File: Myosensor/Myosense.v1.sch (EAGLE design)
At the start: 22 parts, among them IC1 LM358D, IC2 LM358D, IC3 LM358D

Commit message: Worked on myosensor
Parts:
- added JP1: (no value), 3DPC:PINHD-1X2/90
- added OUTPUT: (no value), pinhead:PINHD-1X1
- added SENSOR1, SENSOR2: (no value), pinhead:PINHD-1X2
- IC1, IC2, IC3: value LM358D -> LM358N; device linear:LM358D -> 3DPC:LM358N
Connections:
- net N$9 renamed V2
- new net GND\: SENSOR2.2
- new net V+: IC1P.V+, IC2P.V+, IC3P.V+, JP1.1
- new net V1: IC1A.+IN, SENSOR1.1
- net GND: now also IC1P.V-, IC2P.V-, IC3P.V-, JP1.2, SENSOR1.2
- net N$17: now also OUTPUT.1
- net N$8: now also SENSOR2.1; no longer IC1A.+IN
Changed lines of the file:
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@@
 <layers>
 <layer number="1" name="Top" color="4" fill="1" visible="no" active="no"/>
+<layer number="2" name="Route2" color="1" fill="3" visible="no" active="no"/>
+<layer number="3" name="Route3" color="4" fill="3" visible="no" active="no"/>
+<layer number="4" name="Route4" color="1" fill="4" visible="no" active="no"/>
+<layer number="5" name="Route5" color="4" fill="4" visible="no" active="no"/>
+<layer number="6" name="Route6" color="1" fill="8" visible="no" active="no"/>
+<layer number="7" name="Route7" color="4" fill="8" visible="no" active="no"/>
+<layer number="8" name="Route8" color="1" fill="2" visible="no" active="no"/>
+<layer number="9" name="Route9" color="4" fill="2" visible="no" active="no"/>
+<layer number="10" name="Route10" color="1" fill="7" visible="no" active="no"/>
+<layer number="11" name="Route11" color="4" fill="7" visible="no" active="no"/>
+<layer number="12" name="Route12" color="1" fill="5" visible="no" active="no"/>
+<layer number="13" name="Route13" color="4" fill="5" visible="no" active="no"/>
+<layer number="14" name="Route14" color="1" fill="6" visible="no" active="no"/>
+<layer number="15" name="Route15" color="4" fill="6" visible="no" active="no"/>
 <layer number="16" name="Bottom" color="1" fill="1" visible="no" active="no"/>
 <layer number="17" name="Pads" color="2" fill="1" visible="no" active="no"/>
@@
 </classes>
 <parts>
-<part name="IC1" library="linear" library_urn="urn:adsk.eagle:library:262" deviceset="LM358" device="D" package3d_urn="urn:adsk.eagle:package:16404/2"/>
-<part name="IC2" library="linear" library_urn="urn:adsk.eagle:library:262" deviceset="LM358" device="D" package3d_urn="urn:adsk.eagle:package:16404/2"/>
+<part name="IC1" library="3DPC" deviceset="LM358" device="N" package3d_urn="urn:adsk.eagle:package:16409/2"/>
+<part name="IC2" library="3DPC" deviceset="LM358" device="N" package3d_urn="urn:adsk.eagle:package:16409/2"/>
 <part name="C1" library="capacitor-wima" library_urn="urn:adsk.eagle:library:116" deviceset="C" device="2,5-3" package3d_urn="urn:adsk.eagle:package:5436/1" value="47n"/>
 <part name="C2" library="capacitor-wima" library_urn="urn:adsk.eagle:library:116" deviceset="C" device="2,5-3" package3d_urn="urn:adsk.eagle:package:5436/1" value="47n"/>
@@
 <part name="GND4" library="supply1" library_urn="urn:adsk.eagle:library:371" deviceset="GND" device=""/>
 <part name="GND5" library="supply1" library_urn="urn:adsk.eagle:library:371" deviceset="GND" device=""/>
-<part name="IC3" library="linear" library_urn="urn:adsk.eagle:library:262" deviceset="LM358" device="D" package3d_urn="urn:adsk.eagle:package:16404/2"/>
+<part name="IC3" library="3DPC" deviceset="LM358" device="N" package3d_urn="urn:adsk.eagle:package:16409/2"/>
 <part name="R13" library="rcl" library_urn="urn:adsk.eagle:library:334" deviceset="R-US_" device="0204/5" package3d_urn="urn:adsk.eagle:package:23488/1" value="100"/>
 <part name="R14" library="rcl" library_urn="urn:adsk.eagle:library:334" deviceset="R-US_" device="0204/5" package3d_urn="urn:adsk.eagle:package:23488/1" value="10"/>
+<part name="SENSOR1" library="pinhead" library_urn="urn:adsk.eagle:library:325" deviceset="PINHD-1X2" device="" package3d_urn="urn:adsk.eagle:package:22435/2"/>
+<part name="SENSOR2" library="pinhead" library_urn="urn:adsk.eagle:library:325" deviceset="PINHD-1X2" device="" package3d_urn="urn:adsk.eagle:package:22435/2"/>
+<part name="OUTPUT" library="pinhead" library_urn="urn:adsk.eagle:library:325" deviceset="PINHD-1X1" device="" package3d_urn="urn:adsk.eagle:package:22485/2"/>
+<part name="JP1" library="3DPC" deviceset="PINHD-1X2" device="/90" package3d_urn="urn:adsk.eagle:package:22437/2"/>
 </parts>
 <sheets>
@@
 <attribute name="VALUE" x="92.202" y="41.91" size="1.778" layer="96" rot="R90"/>
 </instance>
+<instance part="SENSOR1" gate="G$1" x="-88.9" y="93.98" smashed="yes">
+<attribute name="NAME" x="-95.25" y="99.695" size="1.778" layer="95"/>
+<attribute name="VALUE" x="-95.25" y="88.9" size="1.778" layer="96"/>
+</instance>
+<instance part="SENSOR2" gate="G$1" x="-88.9" y="50.8" smashed="yes">
+<attribute name="NAME" x="-95.25" y="56.515" size="1.778" layer="95"/>
+<attribute name="VALUE" x="-95.25" y="45.72" size="1.778" layer="96"/>
+</instance>
+<instance part="OUTPUT" gate="G$1" x="137.16" y="66.04" smashed="yes">
+<attribute name="NAME" x="130.81" y="69.215" size="1.778" layer="95"/>
+<attribute name="VALUE" x="130.81" y="60.96" size="1.778" layer="96"/>
+</instance>
+<instance part="IC1" gate="P" x="-60.96" y="93.98" smashed="yes"/>
+<instance part="IC2" gate="P" x="-22.86" y="71.12" smashed="yes"/>
+<instance part="IC3" gate="P" x="101.6" y="66.04" smashed="yes"/>
+<instance part="JP1" gate="G$1" x="-45.72" y="116.84" smashed="yes">
+<attribute name="NAME" x="-52.07" y="122.555" size="1.778" layer="95"/>
+<attribute name="VALUE" x="-52.07" y="111.76" size="1.778" layer="96"/>
+</instance>
 </instances>
 <busses>
@@
 </segment>
 </net>
-<net name="N$8" class="0">
+<net name="V1" class="0">
 <segment>
 <pinref part="IC1" gate="A" pin="+IN"/>
-<wire x1="-68.58" y1="96.52" x2="-78.74" y2="96.52" width="0.1524" layer="91"/>
-</segment>
-</net>
-<net name="N$9" class="0">
+<wire x1="-68.58" y1="96.52" x2="-91.44" y2="96.52" width="0.1524" layer="91"/>
+<label x="-81.28" y="96.52" size="1.778" layer="95"/>
+<pinref part="SENSOR1" gate="G$1" pin="1"/>
+</segment>
+</net>
+<net name="V2" class="0">
 <segment>
 <pinref part="IC1" gate="B" pin="+IN"/>
 <wire x1="-68.58" y1="50.8" x2="-78.74" y2="50.8" width="0.1524" layer="91"/>
+<label x="-81.28" y="50.8" size="1.778" layer="95"/>
 </segment>
 </net>
@@
 <wire x1="88.9" y1="40.64" x2="88.9" y2="38.1" width="0.1524" layer="91"/>
 </segment>
+<segment>
+<pinref part="SENSOR1" gate="G$1" pin="2"/>
+<wire x1="-91.44" y1="93.98" x2="-88.9" y2="93.98" width="0.1524" layer="91"/>
+<wire x1="-88.9" y1="93.98" x2="-88.9" y2="83.82" width="0.1524" layer="91"/>
+<label x="-88.9" y="83.82" size="1.778" layer="95"/>
+</segment>
+<segment>
+<pinref part="JP1" gate="G$1" pin="2"/>
+<wire x1="-48.26" y1="116.84" x2="-35.56" y2="116.84" width="0.1524" layer="91"/>
+<label x="-33.02" y="116.84" size="1.778" layer="95"/>
+</segment>
+<segment>
+<pinref part="IC1" gate="P" pin="V-"/>
+<wire x1="-60.96" y1="86.36" x2="-58.42" y2="86.36" width="0.1524" layer="91"/>
+<label x="-58.42" y="86.36" size="1.778" layer="95"/>
+</segment>
+<segment>
+<pinref part="IC2" gate="P" pin="V-"/>
+<wire x1="-22.86" y1="63.5" x2="-17.78" y2="63.5" width="0.1524" layer="91"/>
+<label x="-17.78" y="63.5" size="1.778" layer="95"/>
+</segment>
+<segment>
+<pinref part="IC3" gate="P" pin="V-"/>
+<wire x1="101.6" y1="58.42" x2="104.14" y2="58.42" width="0.1524" layer="91"/>
+<label x="104.14" y="58.42" size="1.778" layer="95"/>
+</segment>
 </net>
 <net name="N$14" class="0">
@@
 <wire x1="114.3" y1="81.28" x2="114.3" y2="66.04" width="0.1524" layer="91"/>
 <junction x="114.3" y="66.04"/>
-<wire x1="116.84" y1="66.04" x2="121.92" y2="66.04" width="0.1524" layer="91"/>
 <junction x="116.84" y="66.04"/>
-</segment>
-</net>
+<pinref part="OUTPUT" gate="G$1" pin="1"/>
+<wire x1="116.84" y1="66.04" x2="134.62" y2="66.04" width="0.1524" layer="91"/>
+</segment>
+</net>
+<net name="N$8" class="0">
+<segment>
+<wire x1="-81.28" y1="50.8" x2="-86.36" y2="50.8" width="0.1524" layer="91"/>
+<wire x1="-86.36" y1="50.8" x2="-86.36" y2="53.34" width="0.1524" layer="91"/>
+<pinref part="SENSOR2" gate="G$1" pin="1"/>
+<wire x1="-86.36" y1="53.34" x2="-91.44" y2="53.34" width="0.1524" layer="91"/>
+</segment>
+</net>
+<net name="GND\" class="0">
+<segment>
+<pinref part="SENSOR2" gate="G$1" pin="2"/>
+<wire x1="-91.44" y1="50.8" x2="-91.44" y2="43.18" width="0.1524" layer="91"/>
+<label x="-91.44" y="43.18" size="1.778" layer="95"/>
+</segment>
+</net>
+<net name="V+" class="0">
+<segment>
+<pinref part="JP1" gate="G$1" pin="1"/>
+<wire x1="-48.26" y1="119.38" x2="-38.1" y2="119.38" width="0.1524" layer="91"/>
+<label x="-35.56" y="119.38" size="1.778" layer="95"/>
+</segment>
+<segment>
+<pinref part="IC1" gate="P" pin="V+"/>
+<wire x1="-60.96" y1="101.6" x2="-60.96" y2="104.14" width="0.1524" layer="91"/>
+<label x="-58.42" y="104.14" size="1.778" layer="95"/>
+</segment>
+<segment>
+<pinref part="IC2" gate="P" pin="V+"/>
+<wire x1="-22.86" y1="78.74" x2="-20.32" y2="78.74" width="0.1524" layer="91"/>
+<label x="-20.32" y="78.74" size="1.778" layer="95"/>
+</segment>
+<segment>
+<pinref part="IC3" gate="P" pin="V+"/>
+<wire x1="101.6" y1="73.66" x2="104.14" y2="73.66" width="0.1524" layer="91"/>
+<label x="104.14" y="73.66" size="1.778" layer="95"/>
+</segment>
+</net>

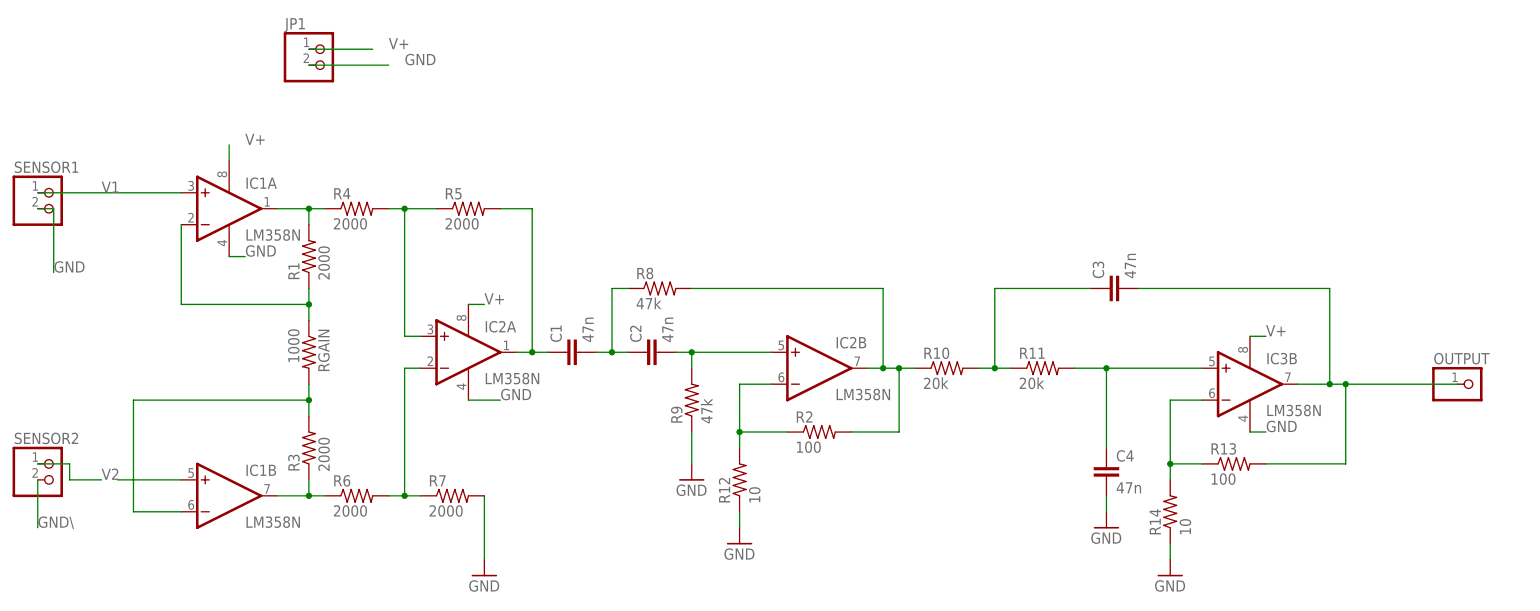
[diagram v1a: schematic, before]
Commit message: Myosensor board and library change
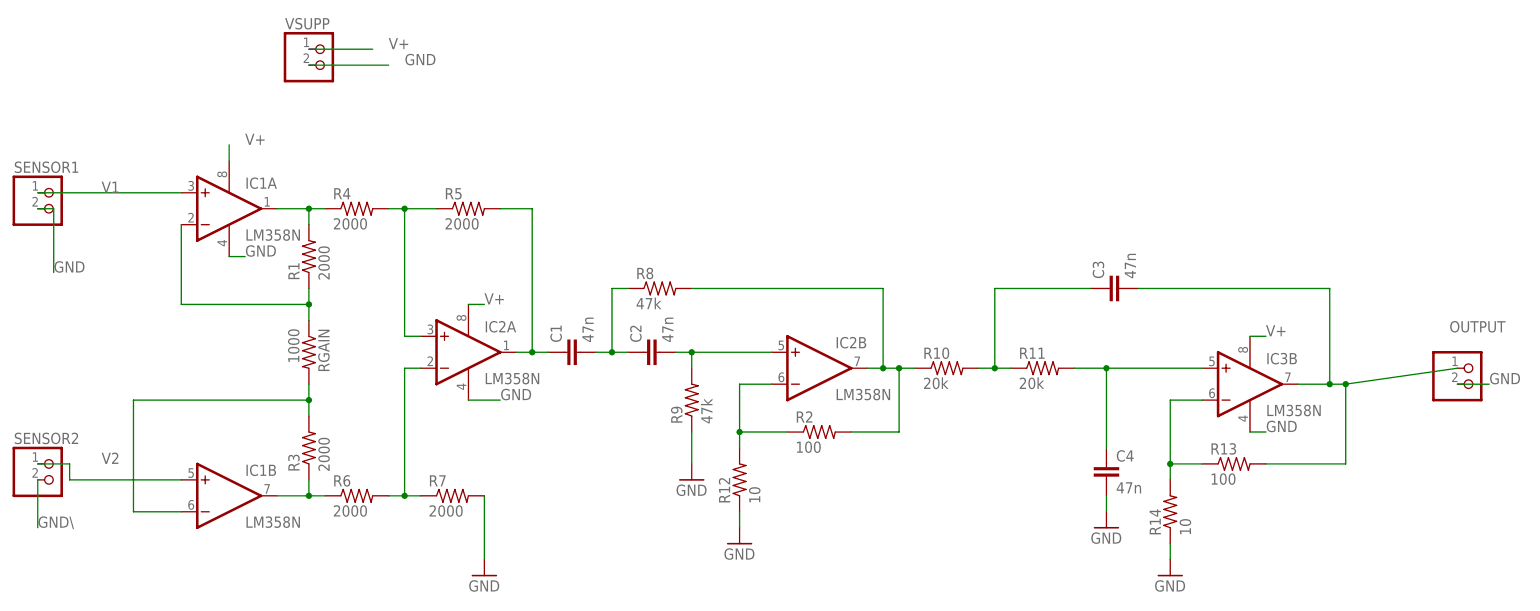
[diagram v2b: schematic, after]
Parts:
- removed JP1: (no value), 3DPC:PINHD-1X2/90
- added VSUPP: (no value), 3DPC:PINHD-1X2
- OUTPUT: device pinhead:PINHD-1X1 -> 3DPC:PINHD-1X2
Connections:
- removed net N$8: SENSOR2.1
- net GND: now also OUTPUT.2, VSUPP.2; no longer JP1.2
- net V+: now also VSUPP.1; no longer JP1.1
- net V2: now also SENSOR2.1
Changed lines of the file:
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@@
 <part name="SENSOR1" library="pinhead" library_urn="urn:adsk.eagle:library:325" deviceset="PINHD-1X2" device="" package3d_urn="urn:adsk.eagle:package:22435/2"/>
 <part name="SENSOR2" library="pinhead" library_urn="urn:adsk.eagle:library:325" deviceset="PINHD-1X2" device="" package3d_urn="urn:adsk.eagle:package:22435/2"/>
-<part name="OUTPUT" library="pinhead" library_urn="urn:adsk.eagle:library:325" deviceset="PINHD-1X1" device="" package3d_urn="urn:adsk.eagle:package:22485/2"/>
-<part name="JP1" library="3DPC" deviceset="PINHD-1X2" device="/90" package3d_urn="urn:adsk.eagle:package:22437/2"/>
+<part name="OUTPUT" library="3DPC" deviceset="PINHD-1X2" device="" package3d_urn="urn:adsk.eagle:package:22435/2"/>
+<part name="VSUPP" library="3DPC" deviceset="PINHD-1X2" device="" package3d_urn="urn:adsk.eagle:package:22435/2"/>
 </parts>
 <sheets>
@@
 </instance>
 <instance part="OUTPUT" gate="G$1" x="137.16" y="66.04" smashed="yes">
-<attribute name="NAME" x="130.81" y="69.215" size="1.778" layer="95"/>
+<attribute name="NAME" x="133.35" y="74.295" size="1.778" layer="95"/>
 <attribute name="VALUE" x="130.81" y="60.96" size="1.778" layer="96"/>
 </instance>
@@
 <instance part="IC2" gate="P" x="-22.86" y="71.12" smashed="yes"/>
 <instance part="IC3" gate="P" x="101.6" y="66.04" smashed="yes"/>
-<instance part="JP1" gate="G$1" x="-45.72" y="116.84" smashed="yes">
+<instance part="VSUPP" gate="G$1" x="-45.72" y="116.84" smashed="yes">
 <attribute name="NAME" x="-52.07" y="122.555" size="1.778" layer="95"/>
 <attribute name="VALUE" x="-52.07" y="111.76" size="1.778" layer="96"/>
@@
 <segment>
 <pinref part="IC1" gate="B" pin="+IN"/>
-<wire x1="-68.58" y1="50.8" x2="-78.74" y2="50.8" width="0.1524" layer="91"/>
-<label x="-81.28" y="50.8" size="1.778" layer="95"/>
+<wire x1="-68.58" y1="50.8" x2="-86.36" y2="50.8" width="0.1524" layer="91"/>
+<label x="-81.28" y="53.34" size="1.778" layer="95"/>
+<wire x1="-86.36" y1="50.8" x2="-86.36" y2="53.34" width="0.1524" layer="91"/>
+<pinref part="SENSOR2" gate="G$1" pin="1"/>
+<wire x1="-86.36" y1="53.34" x2="-91.44" y2="53.34" width="0.1524" layer="91"/>
 </segment>
 </net>
@@
 </segment>
 <segment>
-<pinref part="JP1" gate="G$1" pin="2"/>
+<pinref part="VSUPP" gate="G$1" pin="2"/>
 <wire x1="-48.26" y1="116.84" x2="-35.56" y2="116.84" width="0.1524" layer="91"/>
 <label x="-33.02" y="116.84" size="1.778" layer="95"/>
@@
 <wire x1="101.6" y1="58.42" x2="104.14" y2="58.42" width="0.1524" layer="91"/>
 <label x="104.14" y="58.42" size="1.778" layer="95"/>
+</segment>
+<segment>
+<pinref part="OUTPUT" gate="G$1" pin="2"/>
+<wire x1="134.62" y1="66.04" x2="139.7" y2="66.04" width="0.1524" layer="91"/>
+<label x="139.7" y="66.04" size="1.778" layer="95"/>
 </segment>
 </net>
@@
 <junction x="116.84" y="66.04"/>
 <pinref part="OUTPUT" gate="G$1" pin="1"/>
-<wire x1="116.84" y1="66.04" x2="134.62" y2="66.04" width="0.1524" layer="91"/>
-</segment>
-</net>
-<net name="N$8" class="0">
-<segment>
-<wire x1="-81.28" y1="50.8" x2="-86.36" y2="50.8" width="0.1524" layer="91"/>
-<wire x1="-86.36" y1="50.8" x2="-86.36" y2="53.34" width="0.1524" layer="91"/>
-<pinref part="SENSOR2" gate="G$1" pin="1"/>
-<wire x1="-86.36" y1="53.34" x2="-91.44" y2="53.34" width="0.1524" layer="91"/>
+<wire x1="116.84" y1="66.04" x2="134.62" y2="68.58" width="0.1524" layer="91"/>
 </segment>
 </net>
@@
 <net name="V+" class="0">
 <segment>
-<pinref part="JP1" gate="G$1" pin="1"/>
+<pinref part="VSUPP" gate="G$1" pin="1"/>
 <wire x1="-48.26" y1="119.38" x2="-38.1" y2="119.38" width="0.1524" layer="91"/>
 <label x="-35.56" y="119.38" size="1.778" layer="95"/>
